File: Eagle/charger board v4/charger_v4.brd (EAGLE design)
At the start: 195.2 x 133.3 mm, 62 parts, among them IC1 IR2110D, Q2 IRFP240, Q3 MJE13003G

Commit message: update routing chg
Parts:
- moved C1 5.08 mm to (49.5, 82.5)
- moved C2 5.08 mm to (49.5, 76.2)
- moved D1 1.80 mm to (61.0, 81.3), turned to 0 degrees
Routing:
- net NMOS_SOURCE: track 238.7 -> 243.8 mm
- net 12V: track 32.6 -> 37.6 mm
- net VB: track 25.5 -> 28.0 mm
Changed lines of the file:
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@@
 </autorouter>
 <elements>
-<element name="C1" library="rcl" library_urn="urn:adsk.eagle:library:334" package="C025-025X050" package3d_urn="urn:adsk.eagle:package:23629/2" value="100nF" x="54.61" y="82.55" smashed="yes" rot="R180">
-<attribute name="NAME" x="56.896" y="81.026" size="1.27" layer="25" ratio="10" rot="R180"/>
-<attribute name="POPULARITY" value="65" x="38.1" y="115.57" size="1.778" layer="27" rot="R180" display="off"/>
-<attribute name="SPICEPREFIX" value="C" x="38.1" y="115.57" size="1.778" layer="27" rot="R180" display="off"/>
-<attribute name="VALUE" x="56.896" y="85.344" size="1.27" layer="27" ratio="10" rot="R180"/>
-</element>
-<element name="C2" library="rcl" library_urn="urn:adsk.eagle:library:334" package="E2,5-6E" package3d_urn="urn:adsk.eagle:package:23430/1" value="22uF" x="54.61" y="76.2" smashed="yes" rot="R180">
-<attribute name="NAME" x="51.943" y="74.676" size="1.27" layer="25" ratio="10" rot="R180"/>
-<attribute name="POPULARITY" value="27" x="27.94" y="142.24" size="1.778" layer="27" rot="R180" display="off"/>
-<attribute name="SPICEPREFIX" value="C" x="27.94" y="142.24" size="1.778" layer="27" rot="R180" display="off"/>
-<attribute name="VALUE" x="51.943" y="78.74" size="1.27" layer="27" ratio="10" rot="R180"/>
-</element>
-<element name="D1" library="diode" library_urn="urn:adsk.eagle:library:210" package="DO34-7" package3d_urn="urn:adsk.eagle:package:43348/1" value="UF4007" x="62.23" y="80.01" smashed="yes" rot="R90">
-<attribute name="NAME" x="61.087" y="78.486" size="1.27" layer="25" ratio="10" rot="R90"/>
-<attribute name="POPULARITY" value="2" x="128.27" y="115.57" size="1.778" layer="27" rot="R90" display="off"/>
-<attribute name="VALUE" x="64.643" y="78.486" size="1.27" layer="27" ratio="10" rot="R90"/>
+<element name="C1" library="rcl" library_urn="urn:adsk.eagle:library:334" package="C025-025X050" package3d_urn="urn:adsk.eagle:package:23629/2" value="100nF" x="49.53" y="82.55" smashed="yes" rot="R180">
+<attribute name="NAME" x="51.816" y="81.026" size="1.27" layer="25" ratio="10" rot="R180"/>
+<attribute name="POPULARITY" value="65" x="33.02" y="115.57" size="1.778" layer="27" rot="R180" display="off"/>
+<attribute name="SPICEPREFIX" value="C" x="33.02" y="115.57" size="1.778" layer="27" rot="R180" display="off"/>
+<attribute name="VALUE" x="51.816" y="85.344" size="1.27" layer="27" ratio="10" rot="R180"/>
+</element>
+<element name="C2" library="rcl" library_urn="urn:adsk.eagle:library:334" package="E2,5-6E" package3d_urn="urn:adsk.eagle:package:23430/1" value="22uF" x="49.53" y="76.2" smashed="yes" rot="R180">
+<attribute name="NAME" x="46.863" y="74.676" size="1.27" layer="25" ratio="10" rot="R180"/>
+<attribute name="POPULARITY" value="27" x="22.86" y="142.24" size="1.778" layer="27" rot="R180" display="off"/>
+<attribute name="SPICEPREFIX" value="C" x="22.86" y="142.24" size="1.778" layer="27" rot="R180" display="off"/>
+<attribute name="VALUE" x="46.863" y="78.74" size="1.27" layer="27" ratio="10" rot="R180"/>
+</element>
+<element name="D1" library="diode" library_urn="urn:adsk.eagle:library:210" package="DO34-7" package3d_urn="urn:adsk.eagle:package:43348/1" value="UF4007" x="60.96" y="81.28" smashed="yes">
+<attribute name="NAME" x="59.436" y="82.423" size="1.27" layer="25" ratio="10"/>
+<attribute name="POPULARITY" value="2" x="96.52" y="15.24" size="1.778" layer="27" display="off"/>
+<attribute name="VALUE" x="59.436" y="78.867" size="1.27" layer="27" ratio="10"/>
 </element>
 <element name="D2" library="diode" library_urn="urn:adsk.eagle:library:210" package="DO34-7" package3d_urn="urn:adsk.eagle:package:43348/1" value="UF4007" x="80.01" y="82.55" smashed="yes" rot="R270">
@@
 <contactref element="IC1" pad="6"/>
 <contactref element="C2" pad="+"/>
-<wire x1="62.23" y1="92.71" x2="62.23" y2="88.9" width="1.2192" layer="1"/>
-<wire x1="62.23" y1="88.9" x2="55.88" y2="82.55" width="1.2192" layer="1"/>
-<wire x1="55.88" y1="82.55" x2="55.88" y2="76.2" width="1.2192" layer="1"/>
-<wire x1="55.88" y1="76.2" x2="62.23" y2="76.2" width="0.6096" layer="1"/>
+<wire x1="62.23" y1="92.71" x2="62.23" y2="90.17" width="1.2192" layer="1"/>
+<wire x1="62.23" y1="90.17" x2="57.15" y2="85.09" width="1.2192" layer="1"/>
+<wire x1="57.15" y1="85.09" x2="52.07" y2="85.09" width="1.2192" layer="1"/>
+<wire x1="52.07" y1="85.09" x2="50.8" y2="83.82" width="1.2192" layer="1"/>
+<wire x1="50.8" y1="83.82" x2="50.8" y2="82.55" width="1.2192" layer="1"/>
+<wire x1="50.8" y1="82.55" x2="50.8" y2="76.2" width="1.2192" layer="1"/>
+<wire x1="57.15" y1="85.09" x2="57.15" y2="81.28" width="1.2192" layer="1"/>
 </signal>
 <signal name="NMOS_SOURCE">
@@
 <wire x1="92.557" y1="97.917" x2="92.557" y2="104.293" width="8.89" layer="16"/>
 <wire x1="92.557" y1="104.293" x2="88.9" y2="107.95" width="8.89" layer="16"/>
-<wire x1="59.69" y1="92.71" x2="59.69" y2="90.17" width="1.2192" layer="1"/>
-<wire x1="59.69" y1="90.17" x2="53.34" y2="83.82" width="1.2192" layer="1"/>
-<wire x1="53.34" y1="83.82" x2="53.34" y2="82.55" width="1.2192" layer="1"/>
-<wire x1="53.34" y1="82.55" x2="53.34" y2="76.2" width="1.2192" layer="1"/>
+<wire x1="59.69" y1="92.71" x2="59.69" y2="91.44" width="1.2192" layer="1"/>
+<wire x1="59.69" y1="91.44" x2="55.88" y2="87.63" width="1.2192" layer="1"/>
+<wire x1="55.88" y1="87.63" x2="50.8" y2="87.63" width="1.2192" layer="1"/>
+<wire x1="50.8" y1="87.63" x2="48.26" y2="85.09" width="1.2192" layer="1"/>
+<wire x1="48.26" y1="82.55" x2="48.26" y2="85.09" width="1.2192" layer="1"/>
+<wire x1="48.26" y1="82.55" x2="48.26" y2="76.2" width="1.2192" layer="1"/>
 <wire x1="59.69" y1="92.71" x2="59.69" y2="90.17" width="1.2192" layer="16"/>
 <wire x1="59.69" y1="90.17" x2="63.5" y2="86.36" width="1.2192" layer="16"/>
@@
 <contactref element="ESP" pad="1"/>
 <wire x1="54.61" y1="92.71" x2="54.61" y2="90.17" width="1.2192" layer="16"/>
-<wire x1="54.61" y1="90.17" x2="60.96" y2="83.82" width="1.2192" layer="16"/>
-<wire x1="60.96" y1="83.82" x2="62.23" y2="83.82" width="1.2192" layer="16"/>
-<wire x1="62.7888" y1="84.1248" x2="76.2" y2="97.536" width="0.6096" layer="1"/>
-<wire x1="76.2" y1="97.536" x2="76.2" y2="97.79" width="0.6096" layer="1"/>
-<wire x1="62.7888" y1="84.1248" x2="62.23" y2="83.82" width="0.6096" layer="1"/>
+<wire x1="64.77" y1="81.28" x2="64.77" y2="86.36" width="1.2192" layer="1"/>
+<wire x1="64.77" y1="86.36" x2="76.2" y2="97.79" width="1.2192" layer="1"/>
+<wire x1="64.77" y1="81.28" x2="63.5" y2="81.28" width="1.2192" layer="16"/>
+<wire x1="63.5" y1="81.28" x2="54.61" y2="90.17" width="1.2192" layer="16"/>
 </signal>
 <signal name="V_OUT">

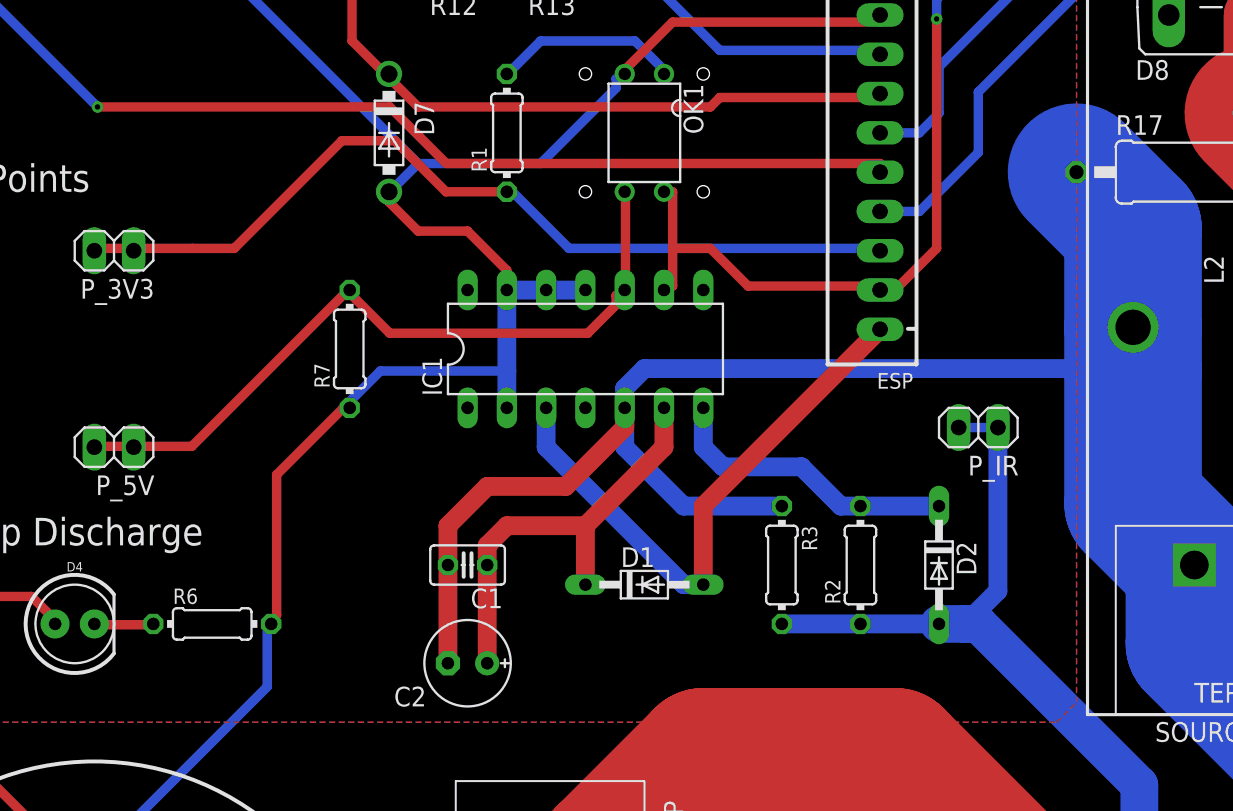
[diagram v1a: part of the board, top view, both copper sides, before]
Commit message: update charger
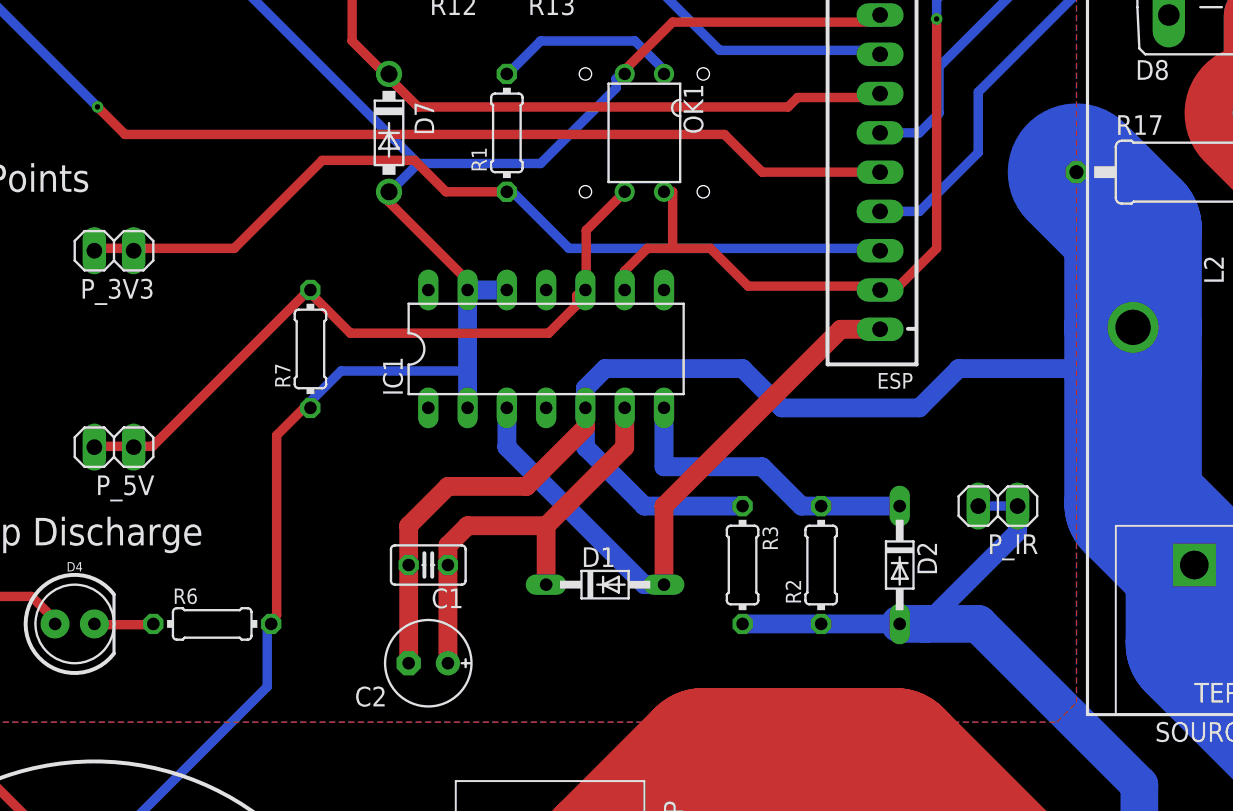
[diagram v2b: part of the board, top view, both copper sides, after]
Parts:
- moved P_IR 5.24 mm to (83.8, 86.4)
- moved D2 2.54 mm to (77.5, 82.5)
- moved R2 2.54 mm to (72.4, 82.5)
- moved C1 2.54 mm to (47.0, 82.5)
- moved C2 2.54 mm to (47.0, 76.2)
- moved D1 2.54 mm to (58.4, 81.3)
- moved IC1 2.54 mm to (54.6, 96.5)
- moved R7 2.54 mm to (39.4, 96.5)
- moved R3 2.54 mm to (67.3, 82.5)
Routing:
- net GND: track 701.6 -> 695.1 mm
- net NMOS_SOURCE: track 243.8 -> 248.4 mm
- net 12V: track 37.6 -> 40.2 mm
- net 5V: track 207.1 -> 209.0 mm
- net PWM_OPTO: track 47.6 -> 46.0 mm
- net PWM_MOSFET: track 56.9 -> 55.8 mm
- net PWM_IR: track 53.3 -> 52.3 mm
- net N$1: track 19.4 -> 20.1 mm
